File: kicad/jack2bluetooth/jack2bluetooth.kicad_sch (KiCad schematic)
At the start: 153 parts, among them IC1 TLV320AIC3101IRHBR, IC2 BQ25619RTWR, IC3 MCP23008T-E_SO, IC4 TPS62A01PDDCR, IC5 TPS62A01PDDCR, IC7 ESP32-WROVER-E-N16R8, J1 SJ3-35063A, J10 Conn_01x03_Pin, J2 USB_C_Receptacle, J3 Conn_01x03_Pin, J4 SJ1-2503A, J5 Conn_01x03_Pin, J6 Conn_01x04_Pin, J7 Conn_01x02_Pin, J8 Conn_01x02_Pin, J9 Conn_01x08_Pin, Q1 DMP3099L-13, Q2 BC846, Q3 BC846, SW1 SW_Push, SW2 SW_Push, SW3 SW_Push, SW4 SW_Push, SW5 SW_SPDT, SW6 SW_Push, SW7 SW_SPDT

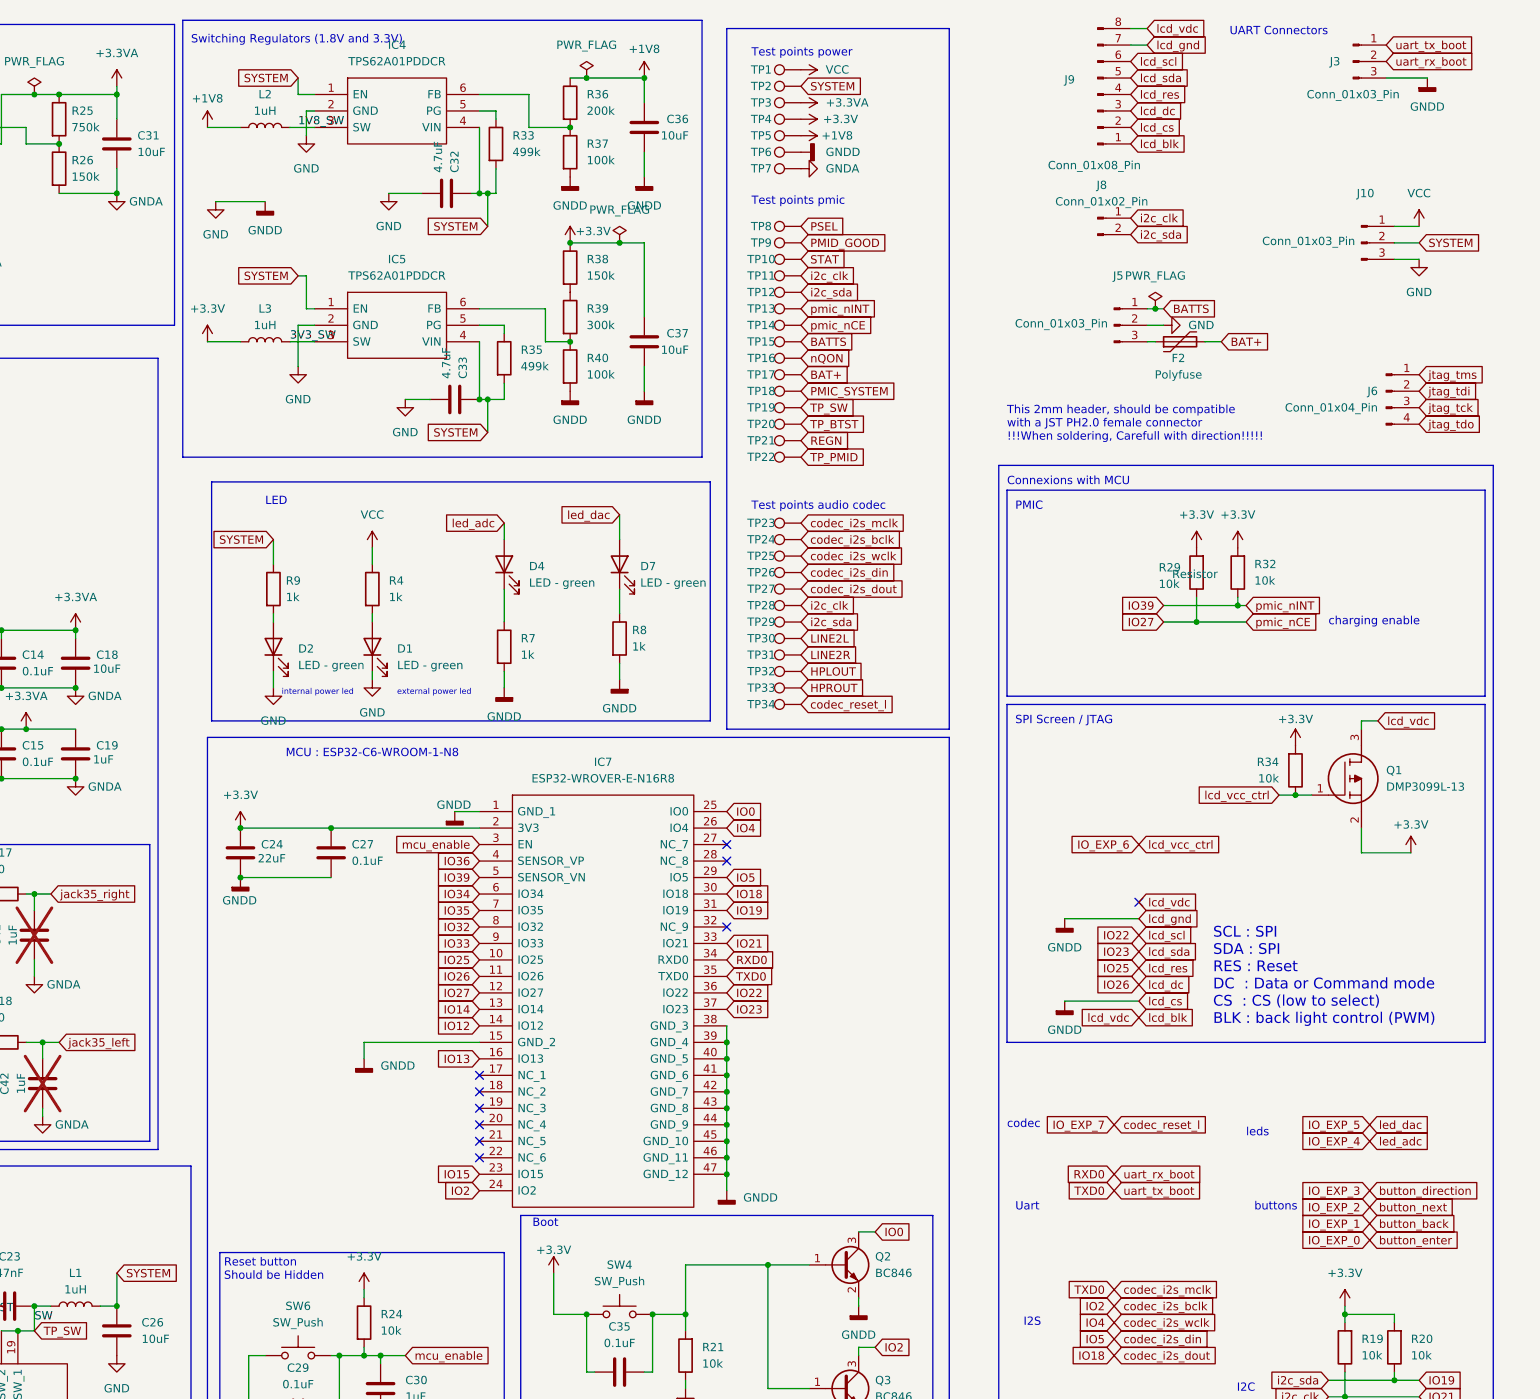
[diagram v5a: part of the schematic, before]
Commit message: feat: finish layout placement
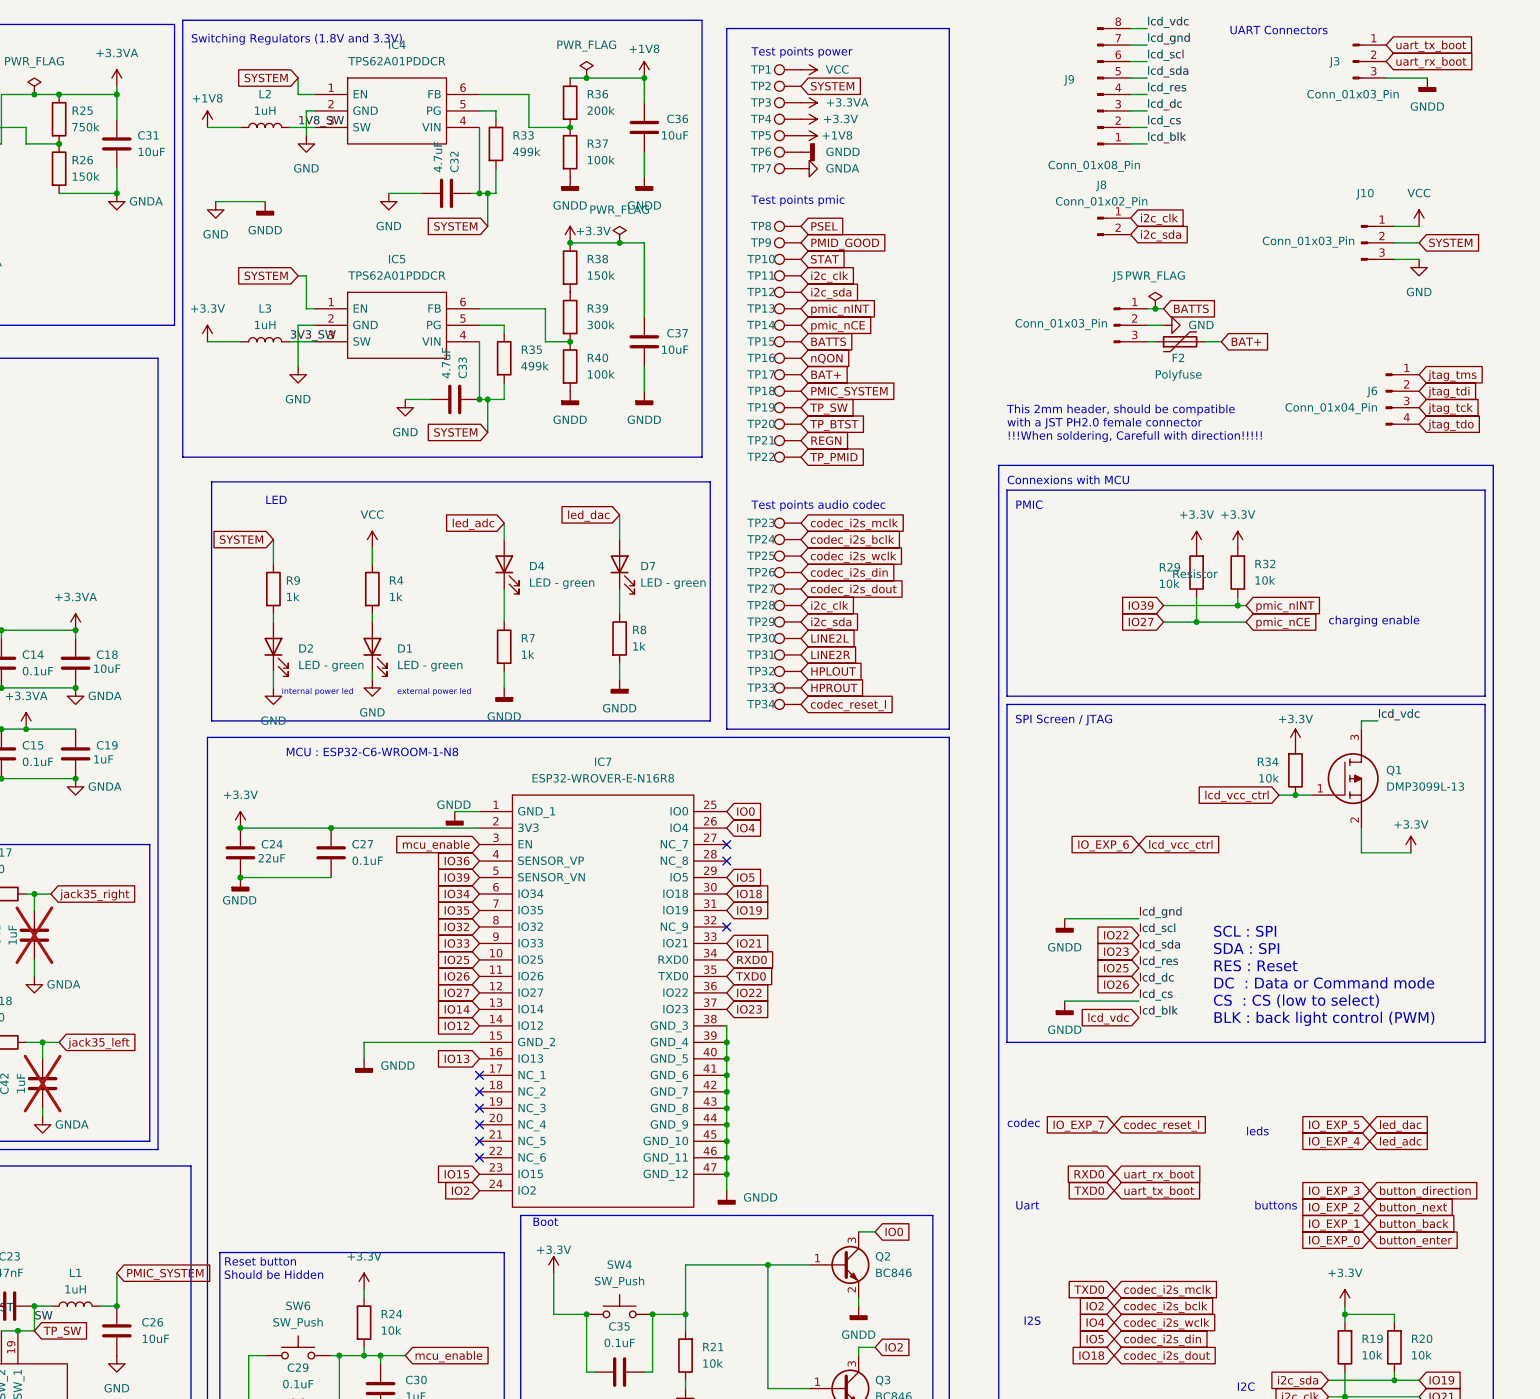
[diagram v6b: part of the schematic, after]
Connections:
- net PMIC_SYSTEM: now also C26.2, L1.2
- net SYSTEM: no longer C26.2, L1.2
- net lcd_blk renamed lcd_vdc
- no-connect marks 37 -> 36

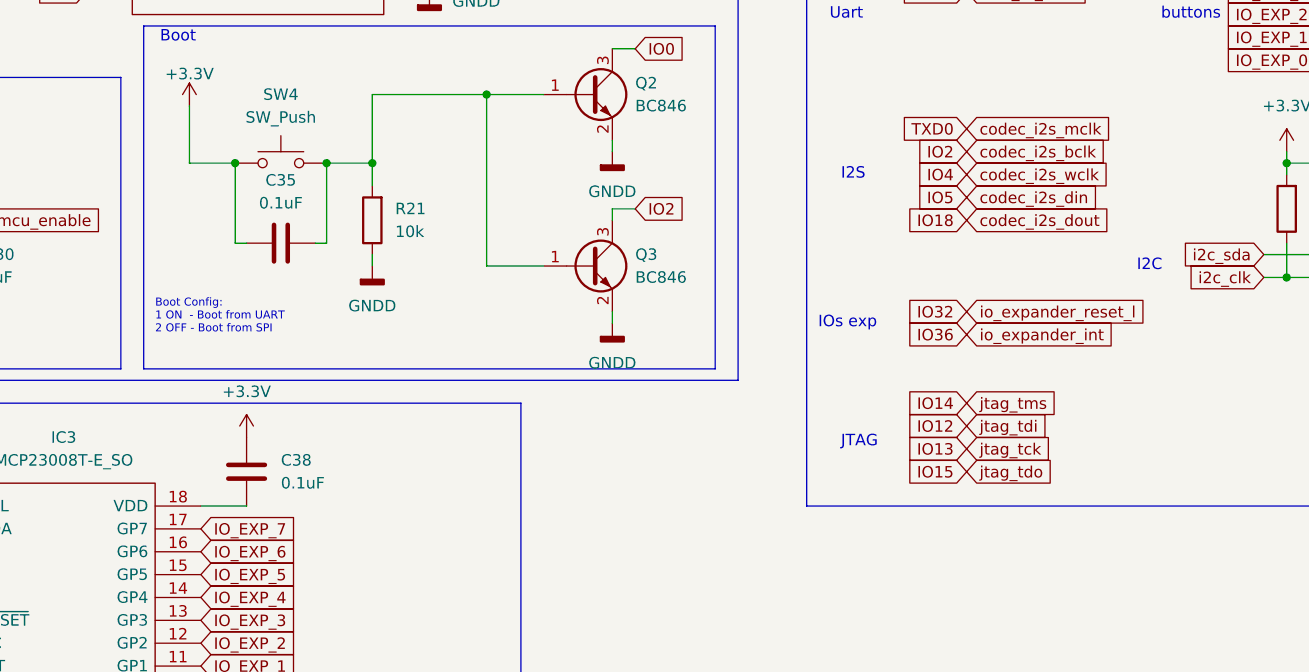
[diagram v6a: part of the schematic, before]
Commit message: feat: update placement and update pin assignments for easier routing
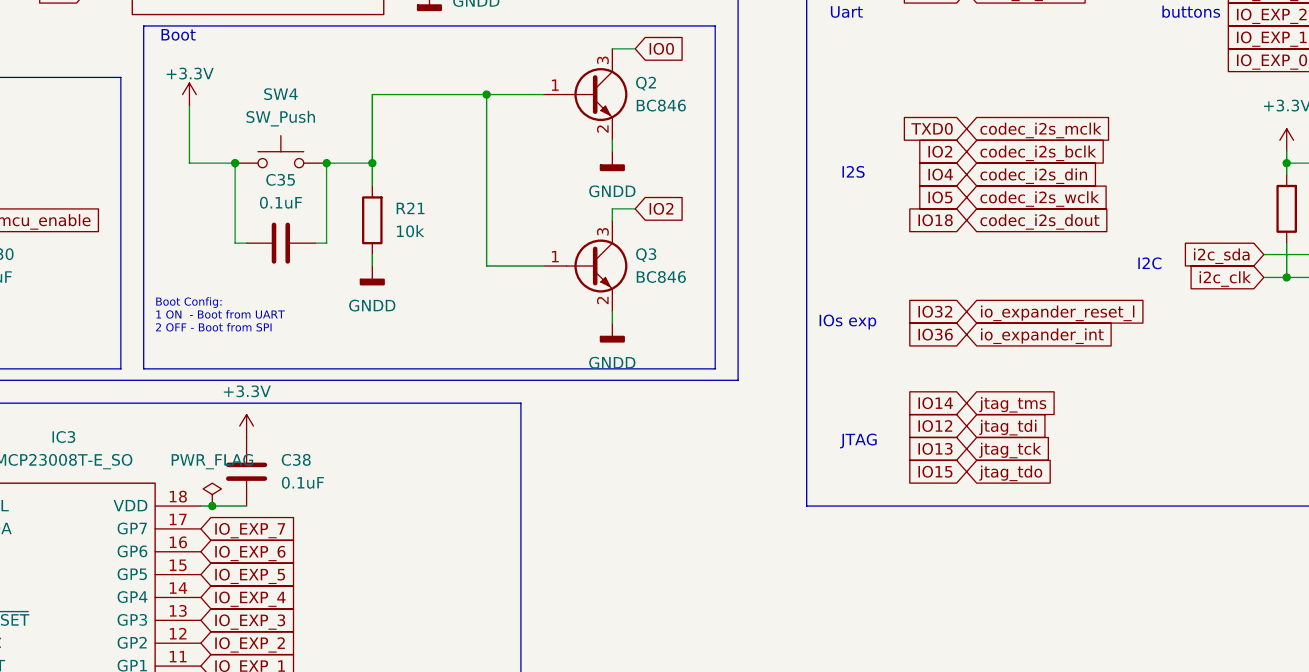
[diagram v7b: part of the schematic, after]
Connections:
- net IO4: now also IC1.4 (DIN), TP26.1; no longer IC1.3 (WCLK), TP25.1
- net IO5: now also IC1.3 (WCLK), TP25.1; no longer IC1.4 (DIN), TP26.1
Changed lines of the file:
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@@
 	)
 	(junction
+		(at 264.16 251.46)
+		(diameter 0)
+		(color 0 0 0 0)
+	)
+	(junction
 		(at 288.29 181.61)
 		(diameter 0)
@@
 	(wire
 		(pts
-			(xy 262.89 251.46) (xy 267.97 251.46)
+			(xy 262.89 251.46) (xy 264.16 251.46)
 		)
 		(stroke
@@
 	(wire
 		(pts
+			(xy 264.16 251.46) (xy 267.97 251.46)
+		)
+		(stroke
+			(width 0)
+			(type default)
+		)
+	)
+	(wire
+		(pts
 			(xy 55.88 46.99) (xy 57.15 46.99)
 		)
@@
 		)
 	)
-	(global_label "codec_i2s_wclk"
-		(shape input)
-		(at 347.98 214.63 0)
-		(fields_autoplaced yes)
-		(effects
-			(font
-				(size 1.27 1.27)
-			)
-			(justify left)
-		)
-		(property "Intersheetrefs" "${INTERSHEET_REFS}"
-			(at 365.419 214.63 0)
-			(effects
-				(font
-					(size 1.27 1.27)
-				)
-				(justify left)
-				(hide yes)
-			)
-		)
-	)
 	(global_label "button_back"
 		(shape input)
@@
 		)
 	)
+	(global_label "codec_i2s_din"
+		(shape input)
+		(at 347.98 214.63 0)
+		(fields_autoplaced yes)
+		(effects
+			(font
+				(size 1.27 1.27)
+			)
+			(justify left)
+		)
+		(property "Intersheetrefs" "${INTERSHEET_REFS}"
+			(at 364.2094 214.63 0)
+			(effects
+				(font
+					(size 1.27 1.27)
+				)
+				(justify left)
+				(hide yes)
+			)
+		)
+	)
 	(global_label "pmic_nINT"
 		(shape input)
@@
 		)
 	)
-	(global_label "IO23"
+	(global_label "codec_i2s_wclk"
 		(shape input)
-		(at 351.79 157.48 180)
+		(at 347.98 217.17 0)
 		(fields_autoplaced yes)
 		(effects
@@
 				(size 1.27 1.27)
 			)
-			(justify right)
+			(justify left)
 		)
 		(property "Intersheetrefs" "${INTERSHEET_REFS}"
-			(at 344.4505 157.48 0)
+			(at 365.419 217.17 0)
 			(effects
 				(font
 					(size 1.27 1.27)
 				)
-				(justify right)
+				(justify left)
 				(hide yes)
 			)
 		)
 	)
-	(global_label "button_next"
+	(global_label "IO23"
 		(shape input)
-		(at 36.83 264.16 180)
+		(at 351.79 157.48 180)
 		(fields_autoplaced yes)
 		(effects
@@
 		)
 		(property "Intersheetrefs" "${INTERSHEET_REFS}"
-			(at 22.8384 264.16 0)
+			(at 344.4505 157.48 0)
 			(effects
 				(font
@@
 		)
 	)
-	(global_label "codec_i2s_din"
+	(global_label "button_next"
 		(shape input)
-		(at 347.98 217.17 0)
+		(at 36.83 264.16 180)
 		(fields_autoplaced yes)
 		(effects
@@
 				(size 1.27 1.27)
 			)
-			(justify left)
+			(justify right)
 		)
 		(property "Intersheetrefs" "${INTERSHEET_REFS}"
-			(at 364.2094 217.17 0)
+			(at 22.8384 264.16 0)
 			(effects
 				(font
 					(size 1.27 1.27)
 				)
-				(justify left)
+				(justify right)
 				(hide yes)
 			)
@@
 					(unit 1)
 				)
+			)
+		)
+	)
+	(symbol
+		(lib_id "power:PWR_FLAG")
+		(at 264.16 251.46 0)
+		(unit 1)
+		(exclude_from_sim no)
+		(in_bom yes)
+		(on_board yes)
+		(dnp no)
+		(fields_autoplaced yes)
+		(property "Reference" "#FLG09"
+			(at 264.16 249.555 0)
+			(effects
+				(font
+					(size 1.27 1.27)
+				)
+				(hide yes)
+			)
+		)
+		(property "Value" "PWR_FLAG"
+			(at 264.16 246.38 0)
+			(effects
+				(font
+					(size 1.27 1.27)
+				)
+			)
+		)
+		(property "Footprint" ""
+			(at 264.16 251.46 0)
+			(effects
+				(font
+					(size 1.27 1.27)
+				)
+				(hide yes)
+			)
+		)
+		(property "Datasheet" "~"
+			(at 264.16 251.46 0)
+			(effects
+				(font
+					(size 1.27 1.27)
+				)
+				(hide yes)
+			)
+		)
+		(property "Description" "Special symbol for telling ERC where power comes from"
+			(at 264.16 251.46 0)
+			(effects
+				(font
+					(size 1.27 1.27)
+				)
+				(hide yes)
+			)
+		)
+		(pin "1"
+		)
+		(instances
+			(project "jack2bluetooth"
+				(path "/4b32d186-730c-41ef-8802-f29516455534"
+					(reference "#FLG09")
+					(unit 1)
+				)
